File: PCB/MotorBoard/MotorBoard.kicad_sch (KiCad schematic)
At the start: 1 part, among them J1 Conn_01x06_Pin

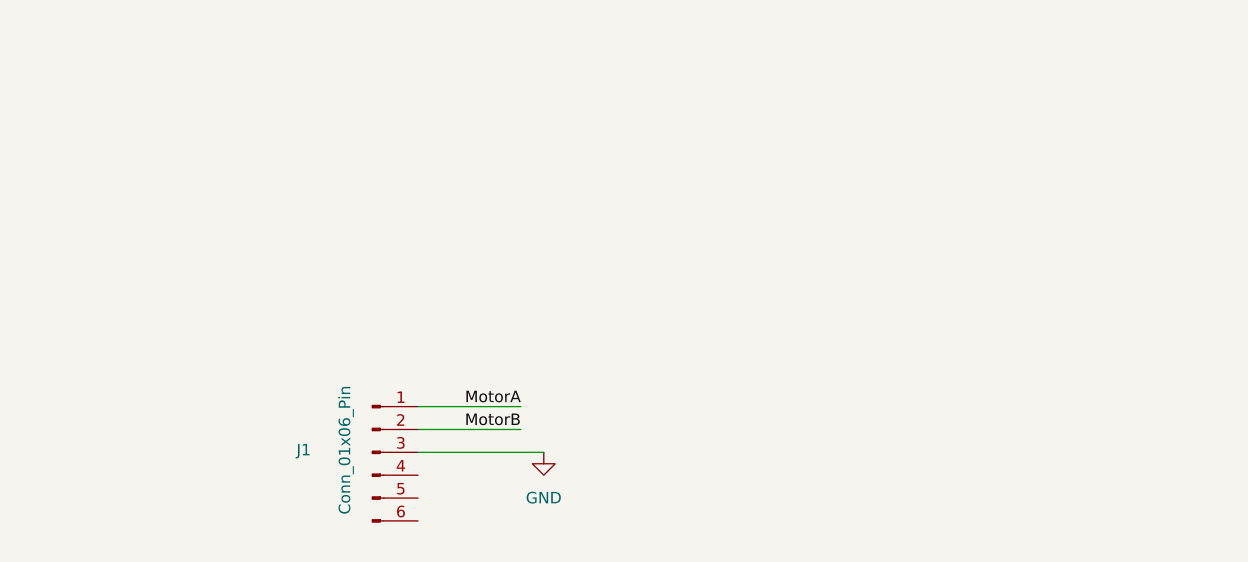
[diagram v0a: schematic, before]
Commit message: Added schematics for motor driver
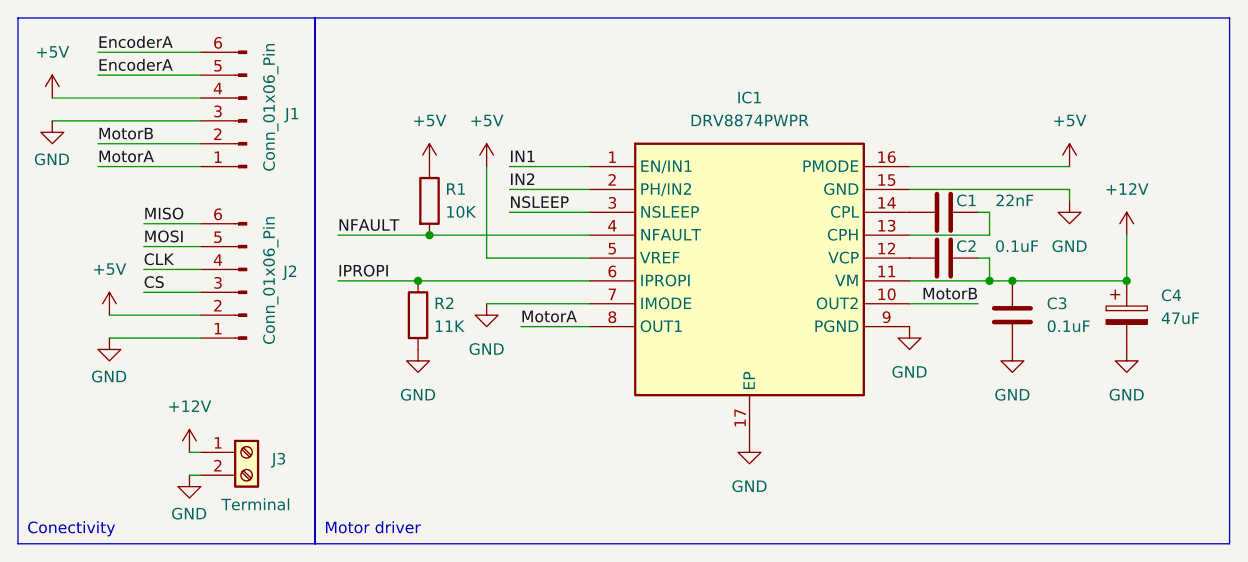
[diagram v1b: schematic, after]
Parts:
- added C1: 22nF, symbol Device:C
- added C2, C3: 0.1uF, symbol Device:C
- added C4: 47uF, symbol Device:C_Polarized
- added IC1: DRV8874PWPR, SOP65P640X120-17N, symbol Components:DRV8874PWPR
- added J2: Conn_01x06_Pin, symbol Connector:Conn_01x06_Pin
- added J3: Terminal, symbol Connector:Screw_Terminal_01x02
- added R1: 10K, symbol Device:R
- added R2: 11K, symbol Device:R
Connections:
- net GND: now also C3.2, C4.2, IC1.15 (GND), IC1.17 (EP), IC1.7 (IMODE), IC1.9 (PGND), J2.1 (Pin_1), J3.2 (Pin_2), R2.2
- net MotorA: now also IC1.8 (OUT1)
- net MotorB: now also IC1.10 (OUT2)
- net +5V: now reaches J1.4 (Pin_4)
- net +5V: now also IC1.16 (PMODE), IC1.5 (VREF), J2.2 (Pin_2), R1.1
- net EncoderA: now reaches J1.5 (Pin_5)
- net EncoderA: now also J1.6 (Pin_6)
- new net: C2.1, IC1.12 (VCP)
- new net: C1.2, IC1.13 (CPH)
- new net: C1.1, IC1.14 (CPL)
- new net +12V: C2.2, C3.1, C4.1, IC1.11 (VM), J3.1 (Pin_1)
- new net CLK: J2.4 (Pin_4)
- new net CS: J2.3 (Pin_3)
- new net IN1: IC1.1 (EN/IN1)
- new net IN2: IC1.2 (PH/IN2)
- new net IPROPI: IC1.6 (IPROPI), R2.1
- new net MISO: J2.6 (Pin_6)
- new net MOSI: J2.5 (Pin_5)
- new net NFAULT: IC1.4 (NFAULT), R1.2
- new net NSLEEP: IC1.3 (NSLEEP)
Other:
- moved on the sheet: J1

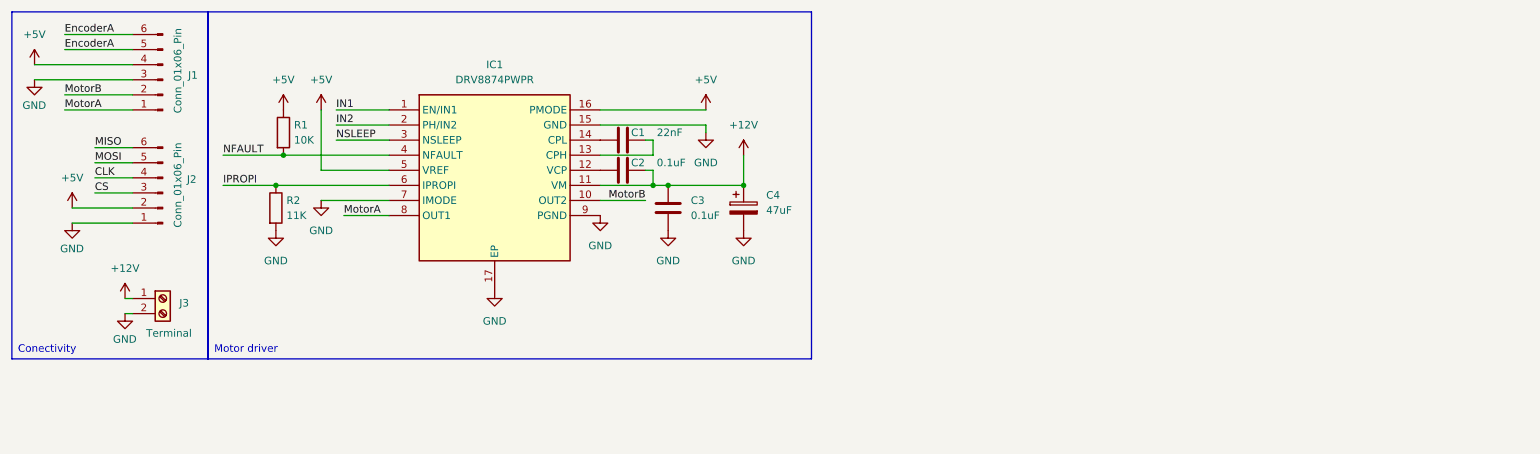
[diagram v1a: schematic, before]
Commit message: Added MCU and started work on it
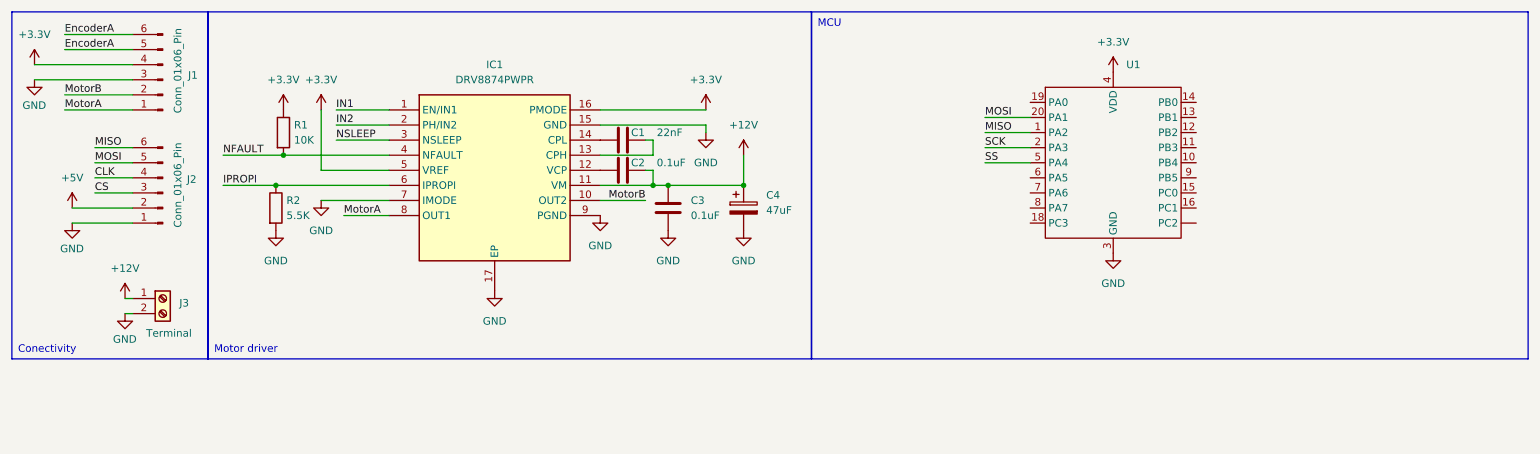
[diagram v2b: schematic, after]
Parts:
- added U1: ~, Package_DFN_QFN:VQFN-20-1EP_3x3mm_P0.4mm_EP1.7x1.7mm, symbol Components:ATTINY417-MN
- R2: value 11K -> 5.5K
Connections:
- net +5V: no longer IC1.16 (PMODE), IC1.5 (VREF), J1.4 (Pin_4), R1.1
- net GND: now also U1.3 (GND)
- net MISO: now also U1.1 (PA2)
- net MOSI: now also U1.20 (PA1)
- new net +3.3V: IC1.16 (PMODE), IC1.5 (VREF), J1.4 (Pin_4), R1.1, U1.4 (VDD)
- new net SCK: U1.2 (PA3)
- new net SS: U1.5 (PA4)

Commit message: MCU scheme done
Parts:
- added C5: C, symbol Device:C
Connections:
- net +3.3V: now also C5.1
- net EncoderA: now also U1.14 (PB0); no longer J1.5 (Pin_5)
- net GND: now also C5.2
- net IN1: now also U1.15 (PC0)
- net IN2: now also U1.16 (PC1)
- net EncoderB: now reaches U1.13 (PB1)
- net EncoderB: now also J1.5 (Pin_5)
- net RESET/UPDI: now reaches U1.19 (PA0)
- no-connect marks 0 -> 2
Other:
- moved on the sheet: U1

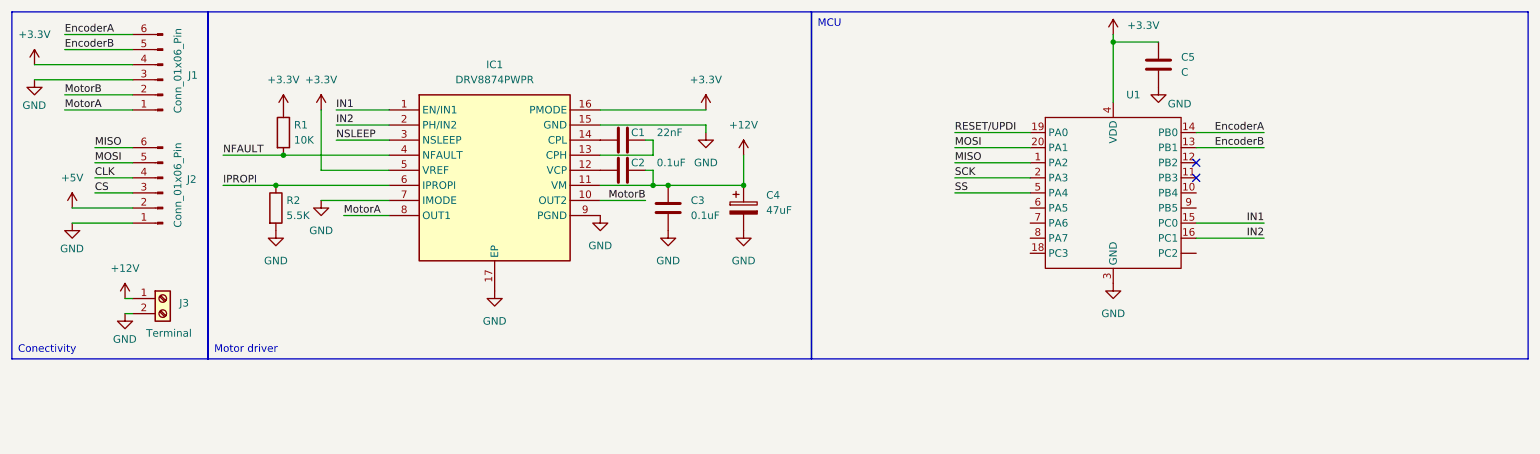
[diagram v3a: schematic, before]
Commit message: Changed to new processor and done schematic for it
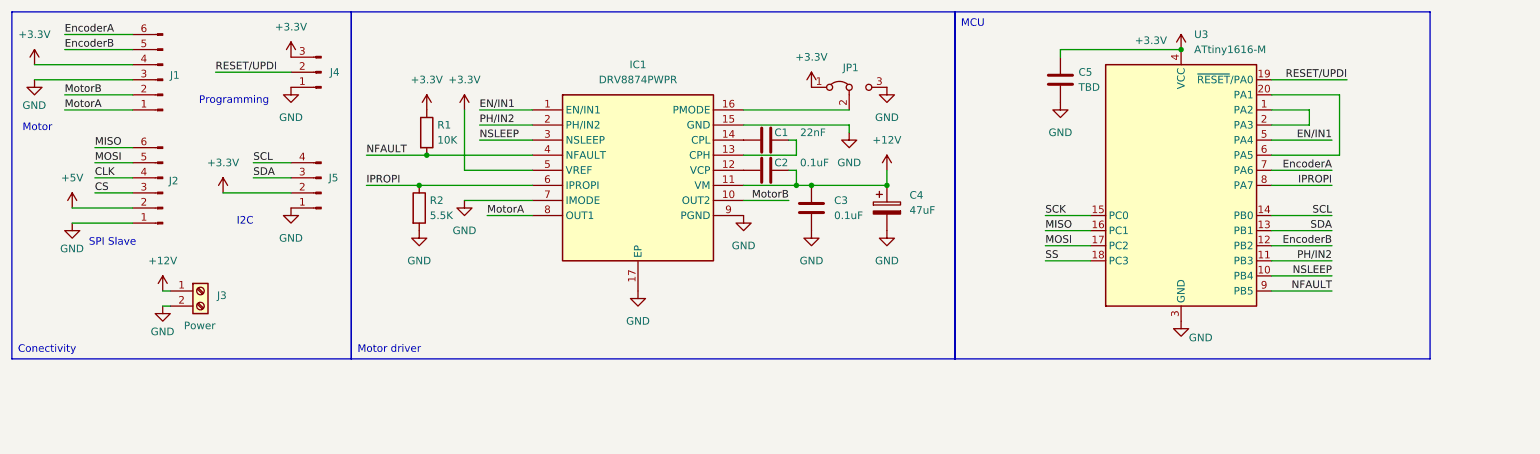
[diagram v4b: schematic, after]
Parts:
- removed U1: ~, Package_DFN_QFN:VQFN-20-1EP_3x3mm_P0.4mm_EP1.7x1.7mm, symbol Components:ATTINY417-MN
- added J4: Conn_01x03_Pin, symbol Connector:Conn_01x03_Pin
- added J5: Conn_01x04_Pin, symbol Connector:Conn_01x04_Pin
- added JP1: Jumper_3_Bridged12, symbol Jumper:Jumper_3_Bridged12
- added U3: ATtiny1616-M, Package_DFN_QFN:VQFN-20-1EP_3x3mm_P0.4mm_EP1.7x1.7mm, symbol MCU_Microchip_ATtiny:ATtiny1616-M
- C5: value C -> TBD
- J3: value Terminal -> Power
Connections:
- net +3.3V: now also J4.3 (Pin_3), J5.2 (Pin_2), JP1.1 (A), U3.4 (VCC); no longer IC1.16 (PMODE)
- net EncoderA: now also U3.7 (PA6)
- net EncoderB: now also U3.12 (PB2)
- net GND: now also J4.1 (Pin_1), J5.1 (Pin_1), JP1.3 (B), U3.21 (GND), U3.3 (GND)
- net IPROPI: now also U3.8 (PA7)
- net MISO: now also U3.16 (PC1)
- net MOSI: now also U3.17 (PC2)
- net NFAULT: now also U3.9 (PB5)
- net NSLEEP: now also U3.10 (PB4)
- net RESET/UPDI: now also J4.2 (Pin_2), U3.19 (~{RESET}/PA0)
- net SCK: now also U3.15 (PC0)
- net SS: now also U3.18 (PC3)
- net IN1 renamed EN/IN1
- net EN/IN1: now also U3.5 (PA4)
- net IN2 renamed PH/IN2
- net PH/IN2: now also U3.11 (PB3)
- new net: IC1.16 (PMODE), JP1.2 (C)
- new net: U3.1 (PA2), U3.2 (PA3)
- new net: U3.20 (PA1), U3.6 (PA5)
- new net SCL: J5.4 (Pin_4), U3.14 (PB0)
- new net SDA: J5.3 (Pin_3), U3.13 (PB1)
- no-connect marks 2 -> 0
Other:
- note added: "I2C"
- note added: "Motor"
- note added: "Programming"
- note added: "SPI Slave"
- moved on the sheet: C1, C2, C3, C4, IC1, J3, R1, R2

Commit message: Changed mcu again
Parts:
- removed U3: ATtiny1616-M, Package_DFN_QFN:VQFN-20-1EP_3x3mm_P0.4mm_EP1.7x1.7mm, symbol MCU_Microchip_ATtiny:ATtiny1616-M
- added J6: Conn_01x04_Pin, symbol Connector:Conn_01x04_Pin
- added U1: ATtiny1617-M, Package_DFN_QFN:QFN-24-1EP_4x4mm_P0.5mm_EP2.6x2.6mm, symbol MCU_Microchip_ATtiny:ATtiny1617-M
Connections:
- net +3.3V: now also J6.2 (Pin_2); no longer C5.1
- net EN/IN1: now also U1.18 (PC1)
- net EncoderA: now also U1.7 (PA6)
- net EncoderB: now also U1.10 (PB6)
- net GND: now also J6.1 (Pin_1), U1.25 (GND), U1.3 (GND)
- net IPROPI: now also U1.24 (PA1)
- net MISO: now also U1.1 (PA2)
- net MOSI: now also U1.19 (PC2)
- net NFAULT: now also U1.13 (PB3)
- net NSLEEP: now also U1.14 (PB2)
- net PH/IN2: now also U1.5 (PA4)
- net RESET/UPDI: now also U1.23 (~{RESET}/PA0)
- net SCK: now also U1.17 (PC0)
- net SCL: now also U1.16 (PB0)
- net SDA: now also U1.15 (PB1)
- net SS: now also U1.20 (PC3)
- new net: C5.1, U1.4 (VCC)
- new net ADC1: J6.4 (Pin_4), U1.11 (PB5)
- new net ADC2: J6.3 (Pin_3), U1.9 (PB7)
- new net A_EDGE: U1.22 (PC5), U1.6 (PA5)
- new net B_EDGE: U1.2 (PA3), U1.21 (PC4)
- no-connect marks 0 -> 2
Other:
- note added: "ADCs"
- moved on the sheet: C5, J3

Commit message: Choosed some packages for components
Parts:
- C1, C2, C3, C4: footprint (none) -> Capacitor_SMD:C_0603_1608Metric
- C5: value TBD -> 10uF; footprint (none) -> Capacitor_Tantalum_SMD:CP_EIA-7343-40_Kemet-Y
- IC1: footprint SOP65P640X120-17N -> Package_SO:HTSSOP-16-1EP_4.4x5mm_P0.65mm_EP3.4x5mm_Mask2.46x2.31mm_ThermalVias
- J2: renamed from J1; footprint (none) -> Connector_PinHeader_2.54mm:PinHeader_1x06_P2.54mm_Vertical
- J3: renamed from J2; footprint (none) -> Connector_JST:JST_XH_B6B-XH-A_1x06_P2.50mm_Vertical
- J4: footprint (none) -> Connector_PinHeader_2.00mm:PinHeader_1x03_P2.00mm_Vertical
- J5, J6: footprint (none) -> Connector_PinHeader_2.00mm:PinHeader_1x04_P2.00mm_Vertical
- JP1: footprint (none) -> Jumper:SolderJumper-3_P1.3mm_Bridged2Bar12_RoundedPad1.0x1.5mm_NumberLabels
- R1: renamed from R2; footprint (none) -> Resistor_SMD:R_0603_1608Metric
- R2: renamed from R1; footprint (none) -> Resistor_SMD:R_0603_1608Metric
- renumbered J3 to J1

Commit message: found all footprints for components
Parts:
- J1: footprint (none) -> Connector_JST:JST_VH_B2P-VH-FB-B_1x02_P3.96mm_Vertical
- J3: footprint Connector_JST:JST_XH_B6B-XH-A_1x06_P2.50mm_Vertical -> Connector_JST:JST_PH_B6B-PH-K_1x06_P2.00mm_Vertical
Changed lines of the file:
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@@
 			)
 		)
-		(property "Footprint" "Connector_JST:JST_XH_B6B-XH-A_1x06_P2.50mm_Vertical"
+		(property "Footprint" "Connector_JST:JST_PH_B6B-PH-K_1x06_P2.00mm_Vertical"
 			(at 43.18 49.53 0)
 			(effects
@@
 			)
 		)
-		(property "Footprint" ""
+		(property "Footprint" "Connector_JST:JST_VH_B2P-VH-FB-B_1x02_P3.96mm_Vertical"
 			(at 40.64 66.04 0)
 			(effects

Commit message: Some minor changes
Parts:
- added C6: 1uF, Capacitor_SMD:C_0603_1608Metric, symbol Device:C
- C4: footprint Capacitor_SMD:C_0603_1608Metric -> Capacitor_Tantalum_SMD:CP_EIA-7343-15_Kemet-W
- C5: value 10uF -> 0.1uF; footprint Capacitor_Tantalum_SMD:CP_EIA-7343-40_Kemet-Y -> Capacitor_SMD:C_0603_1608Metric
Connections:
- net +5V is gone; now on net +3.3V: J3.2 (Pin_2)
- net CLK is gone; now on net SCK: J3.4 (Pin_4)
- net CS is gone; now on net SS: J3.3 (Pin_3)
- net +3.3V: now also C5.1, U1.4 (VCC), C6.1
- net EncoderA: now also U1.10 (PB6); no longer U1.7 (PA6)
- net EncoderB: now also U1.7 (PA6); no longer U1.10 (PB6)
- net GND: now also C6.2
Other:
- moved on the sheet: C5
